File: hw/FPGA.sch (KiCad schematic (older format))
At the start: 35 parts, among them J3 Conn_01x08, SW1 SW_SPST, SW2 SW_SPST, SW3 SW_SPST, U6 ICE40HX4K-TQ144, U7 W25Q128JVS, X2 SG-7050CAN

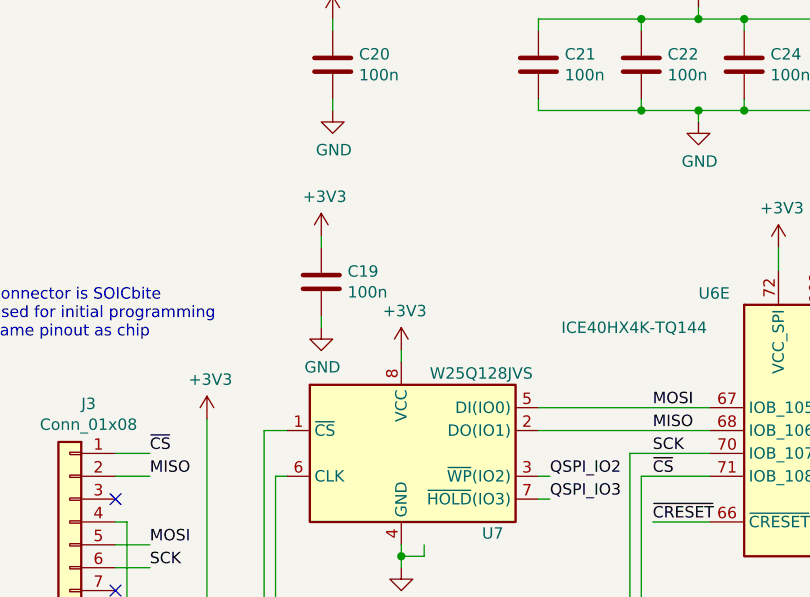
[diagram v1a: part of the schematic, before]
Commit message: Add forgotten pullup to SPI flash ~CS
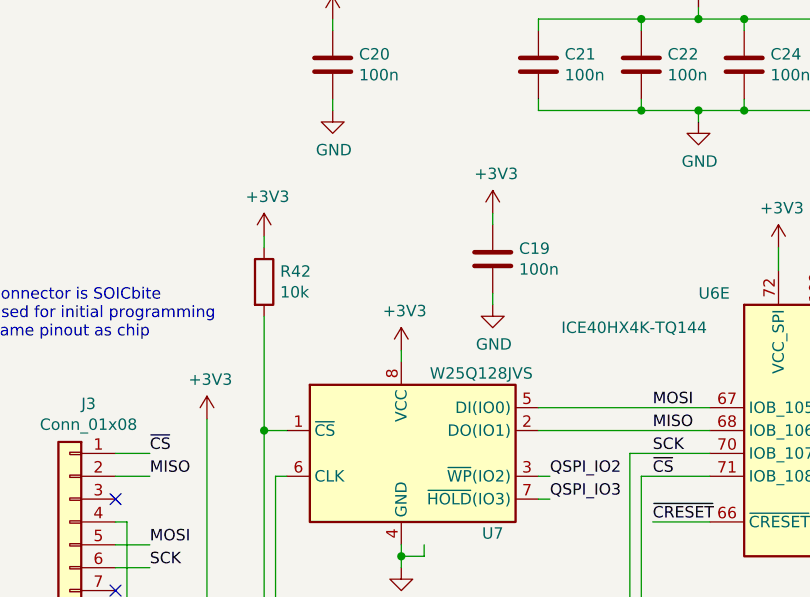
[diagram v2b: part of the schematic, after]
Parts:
- added R42: 10k, Resistor_SMD:R_0603_1608Metric, symbol Device:R
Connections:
- net +3V3: now also R42.1
- net ~CS: now also R42.2
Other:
- moved on the sheet: C19
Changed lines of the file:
@@
 EESchema Schematic File Version 4
+LIBS:manila_ice-cache
 EELAYER 30 0
 EELAYER END
@@
 L Device:C C?
 U 1 1 5D935D29
-P 2000 6050
+P 2750 5950
 AR Path="/5D935D29" Ref="C?"  Part="1"
 AR Path="/5D7E2E67/5D935D29" Ref="C?"  Part="1"
 AR Path="/5D7C5FBE/5D935D29" Ref="C19"  Part="1"
-F 0 "C19" H 2115 6096 50  0000 L CNN
-F 1 "100n" H 2115 6005 50  0000 L CNN
-F 2 "Capacitor_SMD:C_0603_1608Metric" H 2038 5900 50  0001 C CNN
-F 3 "~" H 2000 6050 50  0001 C CNN
-F 4 "C14663" H 2115 6196 50  0001 C CNN "LCSC Part"
-	1    2000 6050
+F 0 "C19" H 2865 5996 50  0000 L CNN
+F 1 "100n" H 2865 5905 50  0000 L CNN
+F 2 "Capacitor_SMD:C_0603_1608Metric" H 2788 5800 50  0001 C CNN
+F 3 "~" H 2750 5950 50  0001 C CNN
+F 4 "C14663" H 2865 6096 50  0001 C CNN "LCSC Part"
+	1    2750 5950
 	1    0    0    -1
 $EndComp
@@
 L power:+3V3 #PWR062
 U 1 1 5D935D2F
-P 2000 5850
-F 0 "#PWR062" H 2000 5700 50  0001 C CNN
-F 1 "+3V3" H 2015 6023 50  0000 C CNN
-F 2 "" H 2000 5850 50  0001 C CNN
-F 3 "" H 2000 5850 50  0001 C CNN
-	1    2000 5850
+P 1750 5850
+F 0 "#PWR062" H 1750 5700 50  0001 C CNN
+F 1 "+3V3" H 1765 6023 50  0000 C CNN
+F 2 "" H 1750 5850 50  0001 C CNN
+F 3 "" H 1750 5850 50  0001 C CNN
+	1    1750 5850
 	1    0    0    -1
 $EndComp
@@
 L power:GND #PWR063
 U 1 1 5D935D35
-P 2000 6250
-F 0 "#PWR063" H 2000 6000 50  0001 C CNN
-F 1 "GND" H 2005 6077 50  0000 C CNN
-F 2 "" H 2000 6250 50  0001 C CNN
-F 3 "" H 2000 6250 50  0001 C CNN
-	1    2000 6250
+P 2750 6150
+F 0 "#PWR063" H 2750 5900 50  0001 C CNN
+F 1 "GND" H 2755 5977 50  0000 C CNN
+F 2 "" H 2750 6150 50  0001 C CNN
+F 3 "" H 2750 6150 50  0001 C CNN
+	1    2750 6150
 	1    0    0    -1
 $EndComp
@@
 	3400 6900 3700 6900
 Wire Wire Line
-	2000 5850 2000 5900
-Wire Wire Line
-	2000 6200 2000 6250
+	2750 5750 2750 5800
+Wire Wire Line
+	2750 6100 2750 6150
 Wire Wire Line
 	9250 2950 9750 2950
@@
 Wire Wire Line
 	750  3350 1250 3350
+Text HLabel 750  3350 0    50   BiDi ~ 0
+SDA
+Text HLabel 750  3250 0    50   BiDi ~ 0
+SCL
+$Comp
+L Device:R R42
+U 1 1 5DACEAF4
+P 1750 6050
+F 0 "R42" H 1820 6096 50  0000 L CNN
+F 1 "10k" H 1820 6005 50  0000 L CNN
+F 2 "Resistor_SMD:R_0603_1608Metric" V 1680 6050 50  0001 C CNN
+F 3 "~" H 1750 6050 50  0001 C CNN
+F 4 "C25804" H 1820 6196 50  0001 C CNN "LCSC Part"
+	1    1750 6050
+	1    0    0    -1
+$EndComp
+$Comp
+L power:+3V3 #PWR0134
+U 1 1 5DB10ADD
+P 2750 5750
+F 0 "#PWR0134" H 2750 5600 50  0001 C CNN
+F 1 "+3V3" H 2765 5923 50  0000 C CNN
+F 2 "" H 2750 5750 50  0001 C CNN
+F 3 "" H 2750 5750 50  0001 C CNN
+	1    2750 5750
+	1    0    0    -1
+$EndComp
+Wire Wire Line
+	1750 5850 1750 5900
+Wire Wire Line
+	1750 6200 1750 6700
 Wire Bus Line
 	5600 3800 5600 4650
@@
 Wire Bus Line
 	5500 1550 5500 2900
-Text HLabel 750  3350 0    50   BiDi ~ 0
-SDA
-Text HLabel 750  3250 0    50   BiDi ~ 0
-SCL
+Connection ~ 1750 6700
 $EndSCHEMATC

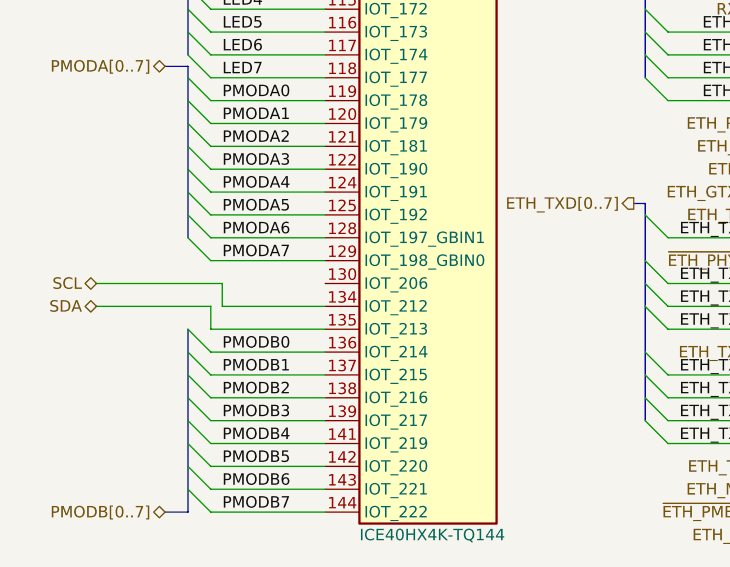
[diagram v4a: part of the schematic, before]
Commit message: Fixed tant footprint. Added JLC part numbers to other components
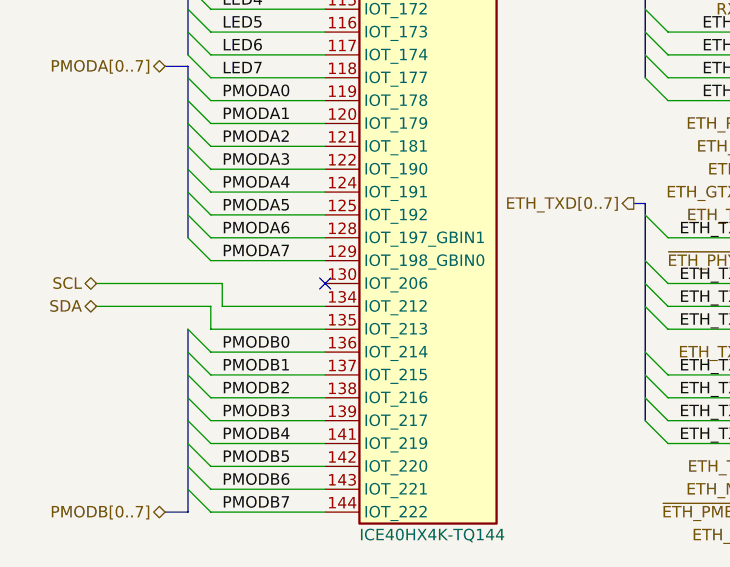
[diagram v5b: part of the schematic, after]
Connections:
- no-connect marks 3 -> 4

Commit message: Fix JLC rotation
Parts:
- C18, C19, C20, C21, C22, C23, C24, C25, C26, C27, C28, C29, C30, C31, C32, C33, C34, C35, C36, C37, D3, R25, R26, R27, R28, R29, R30, R31, R42, SW1, SW2, SW3, X2: JLCPCB Rotation (none) -> 0
- U7: JLCPCB Rotation (none) -> -90

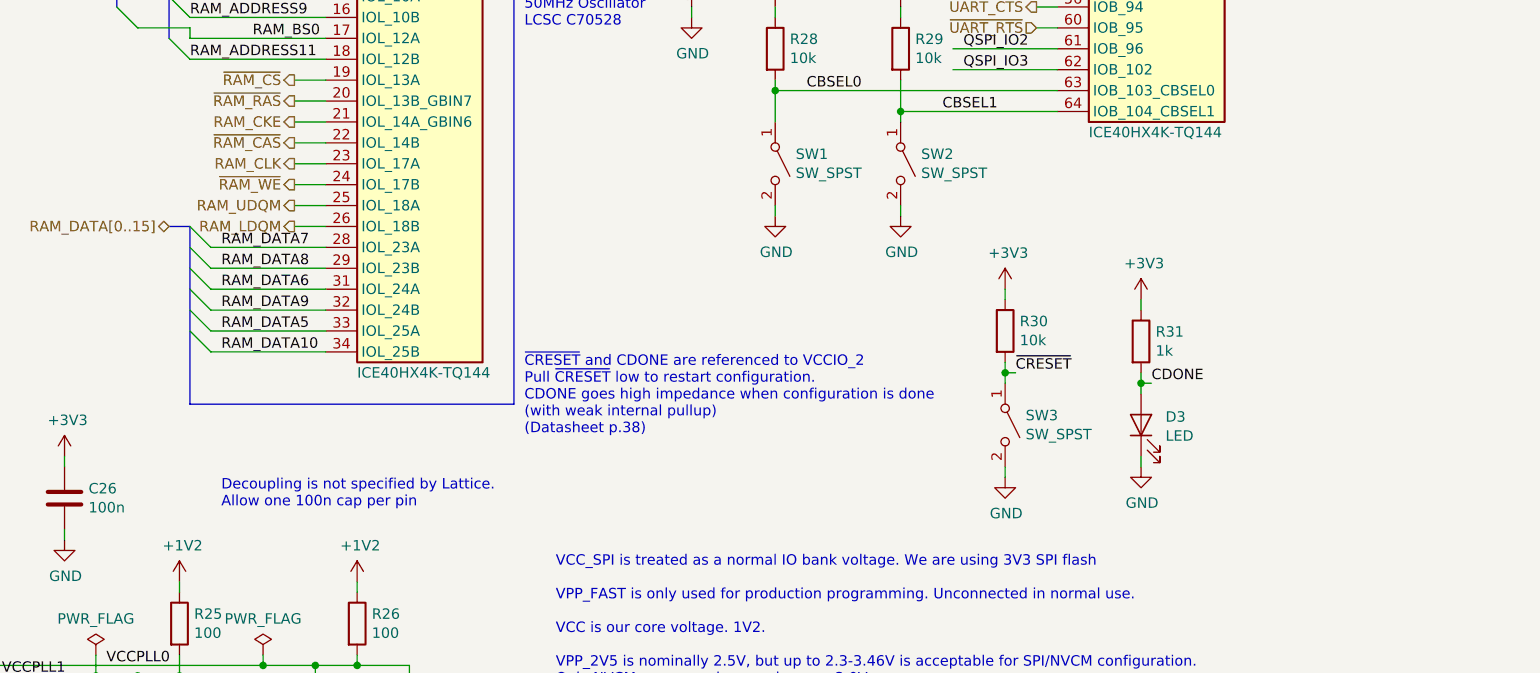
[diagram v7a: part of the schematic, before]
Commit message: Update schematic to change slew rates of PSUs and to add switch debouncing
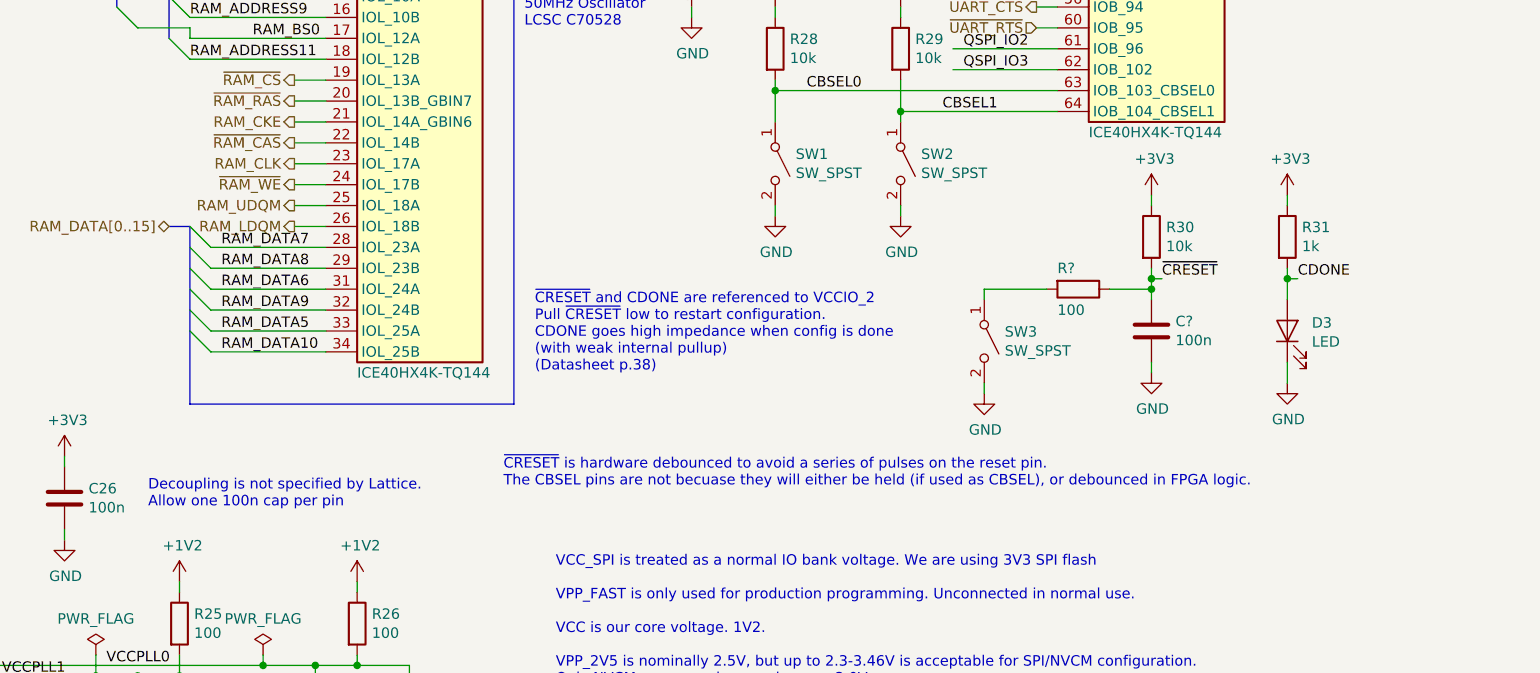
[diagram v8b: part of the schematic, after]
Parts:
- added C?: 100n, Capacitor_SMD:C_0603_1608Metric, symbol Device:C
- added R?: 100, Resistor_SMD:R_0603_1608Metric, symbol Device:R
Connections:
- net GND: now also C?.2
- net ~CRESET: now also C?.1, R?.1; no longer SW3.1 (A)
- new net: R?.2, SW3.1 (A)
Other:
- note added: "~CRESET~ and CDONE are referenced to VCCIO_2\nPull ~CRESET~ low to restart configuration.\nCDONE goes high impedance when config is done\n(with weak internal pullup) \n(Datasheet p.38)"
- note added: "~CRESET~ is hardware debounced to avoid a series of pulses on the reset pin.\nThe CBSEL pins are not becuase they will either be held (if used as CBSEL), or debounced in FPGA logic."
- note removed: "~CRESET~ and CDONE are referenced to VCCIO_2\nPull ~CRESET~ low to restart configuration.\nCDONE goes high impedance when configuration is done\n(with weak internal pullup) \n(Datasheet p.38)"
- moved on the sheet: D3, R30, R31, SW3
